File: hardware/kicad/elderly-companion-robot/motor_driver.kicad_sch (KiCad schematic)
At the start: 12 parts, among them J3 Motor_A, J4 Motor_B, U5 L298N

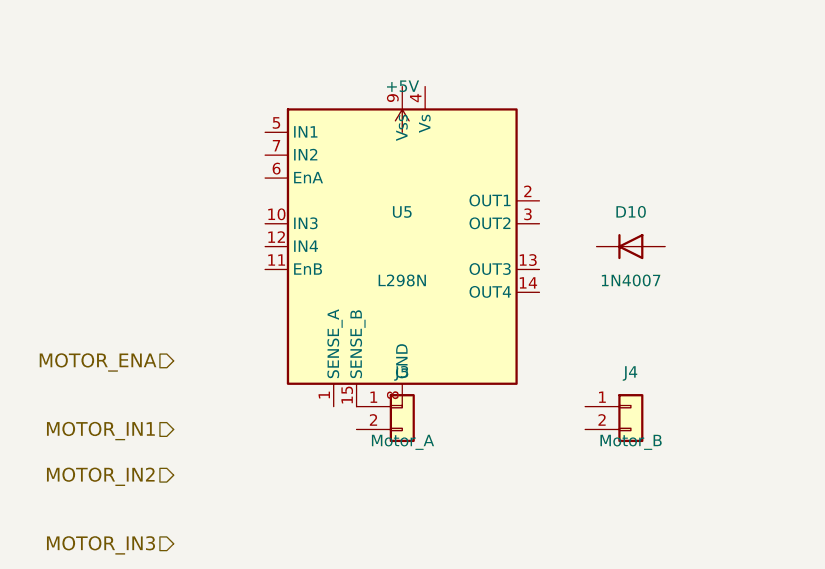
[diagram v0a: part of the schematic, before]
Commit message: Add net labels and signal connections across all schematic sheets
- MCU Core: Added net labels at all ESP32-S3 GPIO pin positions
  (I2C, I2S, motor, servo, IR, UART, ultrasonic signals)
- Added hierarchical labels for US_LEFT/RIGHT_TRIG/ECHO
- Remapped I2C_SCL to GPIO2 (GPIO22 not on WROOM-1 module)
- Remapped SERVO_PAN to GPIO42 (GPIO44 not available)
- Motor Driver: Added net labels at L298N input/output pins
- Sensors: Added I2C labels at MPU-6050 and SSD1306 pin positions
- Audio: Added I2S labels at MAX98357A and INMP441 connector
- Camera/Dock: Added UART, SIM_PWRKEY, servo, IR labels at SIM800C
- Added power symbols (+3V3, +5V, GND, +4V) across all sheets
- Boot circuit wiring started (EN pull-up, GPIO0 connections)
- ERC: 446 violations (mostly unconnected labels/pins - need wires)

Co-Authored-By: Claude Opus 4.7 <noreply@anthropic.com>
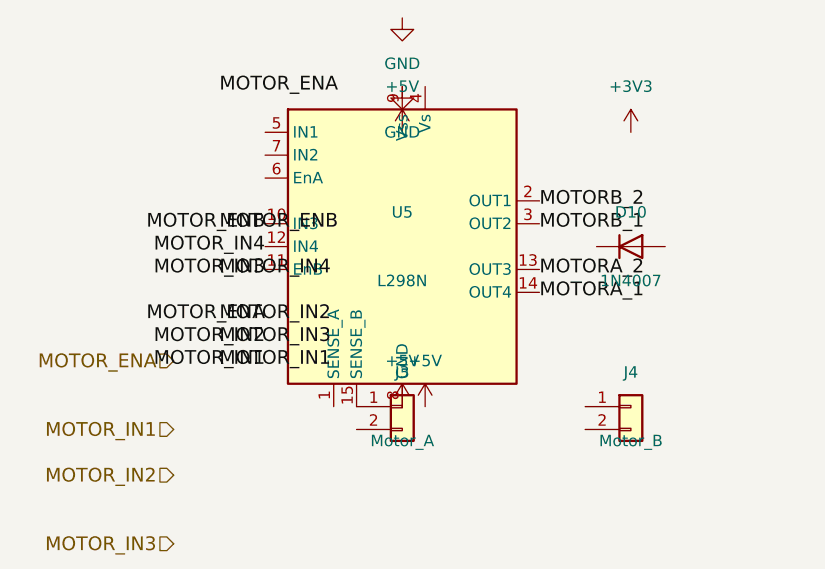
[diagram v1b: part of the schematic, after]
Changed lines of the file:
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@@
 	(version 20250114)
 	(generator "eeschema")
+	(generator_version "9.0")
 	(paper "A4")
 	(symbol
@@
 		(effects (font (size 1.524 1.524)))
 	)
+	(symbol
+		(lib_id "power:+5V")
+		(at 50.8 68.58 0)
+		(unit 1)
+		(exclude_from_sim no)
+		(in_bom yes)
+		(on_board yes)
+		(dnp no)
+		(property "Reference" "#PWR3f77"
+			(at 50.8 62.23 0)
+			(effects (font (size 1.27 1.27)) (hide yes))
+		)
+		(property "Value" "+5V"
+			(at 50.8 63.5 0)
+			(effects (font (size 1.27 1.27)))
+		)
+		(property "Footprint" ""
+			(at 50.8 68.58 0)
+			(effects (font (size 1.27 1.27)) (hide yes))
+		)
+		(property "Datasheet" "~"
+			(at 50.8 68.58 0)
+			(effects (font (size 1.27 1.27)) (hide yes))
+		)
+		(instances
+			(project "elderly-companion-robot"
+				(path "/4df18afa-6300-4e30-8425-a36b74deadc2"
+					(reference "#PWR3f77") (unit 1)
+				)
+			)
+		)
+	)
+	(symbol
+		(lib_id "power:+3V3")
+		(at 76.2 38.1 0)
+		(unit 1)
+		(exclude_from_sim no)
+		(in_bom yes)
+		(on_board yes)
+		(dnp no)
+		(property "Reference" "#PWR25e6"
+			(at 76.2 31.75 0)
+			(effects (font (size 1.27 1.27)) (hide yes))
+		)
+		(property "Value" "+3V3"
+			(at 76.2 33.02 0)
+			(effects (font (size 1.27 1.27)))
+		)
+		(property "Footprint" ""
+			(at 76.2 38.1 0)
+			(effects (font (size 1.27 1.27)) (hide yes))
+		)
+		(property "Datasheet" "~"
+			(at 76.2 38.1 0)
+			(effects (font (size 1.27 1.27)) (hide yes))
+		)
+		(instances
+			(project "elderly-companion-robot"
+				(path "/d9fcf0f2-e47a-435c-a687-ceb3313aee18"
+					(reference "#PWR25e6") (unit 1)
+				)
+			)
+		)
+	)
+	(symbol
+		(lib_id "power:GND")
+		(at 50.8 25.4 0)
+		(unit 1)
+		(exclude_from_sim no)
+		(in_bom yes)
+		(on_board yes)
+		(dnp no)
+		(property "Reference" "#PWR14a6"
+			(at 50.8 31.75 0)
+			(effects (font (size 1.27 1.27)) (hide yes))
+		)
+		(property "Value" "GND"
+			(at 50.8 30.48 0)
+			(effects (font (size 1.27 1.27)))
+		)
+		(property "Footprint" ""
+			(at 50.8 25.4 0)
+			(effects (font (size 1.27 1.27)) (hide yes))
+		)
+		(property "Datasheet" "~"
+			(at 50.8 25.4 0)
+			(effects (font (size 1.27 1.27)) (hide yes))
+		)
+		(instances
+			(project "elderly-companion-robot"
+				(path "/d9c6cb88-2fe3-4b29-b416-8258e6ea7698"
+					(reference "#PWR14a6") (unit 1)
+				)
+			)
+		)
+	)
+	(label "MOTOR_ENA"
+		(at 30.48 33.02 0)
+		(effects (font (size 1.524 1.524)))
+	)
+	(label "MOTOR_IN1"
+		(at 30.48 63.5 0)
+		(effects (font (size 1.524 1.524)))
+	)
+	(label "MOTOR_IN2"
+		(at 30.48 58.42 0)
+		(effects (font (size 1.524 1.524)))
+	)
+	(label "MOTOR_IN3"
+		(at 30.48 60.96 0)
+		(effects (font (size 1.524 1.524)))
+	)
+	(label "MOTOR_IN4"
+		(at 30.48 53.34 0)
+		(effects (font (size 1.524 1.524)))
+	)
+	(label "MOTOR_ENB"
+		(at 30.48 48.26 0)
+		(effects (font (size 1.524 1.524)))
+	)
+	(label "MOTOR_IN1"
+		(at 35.56 63.5 180)
+		(effects (font (size 1.524 1.524)))
+	)
+	(label "MOTOR_IN2"
+		(at 35.56 60.96 180)
+		(effects (font (size 1.524 1.524)))
+	)
+	(label "MOTOR_IN3"
+		(at 35.56 53.34 180)
+		(effects (font (size 1.524 1.524)))
+	)
+	(label "MOTOR_IN4"
+		(at 35.56 50.8 180)
+		(effects (font (size 1.524 1.524)))
+	)
+	(label "MOTOR_ENA"
+		(at 35.56 58.42 180)
+		(effects (font (size 1.524 1.524)))
+	)
+	(label "MOTOR_ENB"
+		(at 35.56 48.26 180)
+		(effects (font (size 1.524 1.524)))
+	)
+	(label "MOTORA_1"
+		(at 66.04 55.88 0)
+		(effects (font (size 1.524 1.524)))
+	)
+	(label "MOTORA_2"
+		(at 66.04 53.34 0)
+		(effects (font (size 1.524 1.524)))
+	)
+	(label "MOTORB_1"
+		(at 66.04 48.26 0)
+		(effects (font (size 1.524 1.524)))
+	)
+	(label "MOTORB_2"
+		(at 66.04 45.72 0)
+		(effects (font (size 1.524 1.524)))
+	)
+	(symbol
+		(lib_id "power:+5V")
+		(at 53.34 68.58 0)
+		(unit 1)
+		(exclude_from_sim no)
+		(in_bom yes)
+		(on_board yes)
+		(dnp no)
+		(property "Reference" "#PWRf70d"
+			(at 53.34 62.23 0)
+			(effects (font (size 1.27 1.27)) (hide yes))
+		)
+		(property "Value" "+5V"
+			(at 53.34 63.5 0)
+			(effects (font (size 1.27 1.27)))
+		)
+		(property "Footprint" ""
+			(at 53.34 68.58 0)
+			(effects (font (size 1.27 1.27)) (hide yes))
+		)
+		(property "Datasheet" "~"
+			(at 53.34 68.58 0)
+			(effects (font (size 1.27 1.27)) (hide yes))
+		)
+		(instances
+			(project "elderly-companion-robot"
+				(path "/31d9b13f-5923-4cd5-9096-a5c3c0de11a9"
+					(reference "#PWRf70d") (unit 1)
+				)
+			)
+		)
+	)
+	(symbol
+		(lib_id "power:GND")
+		(at 50.8 33.02 0)
+		(unit 1)
+		(exclude_from_sim no)
+		(in_bom yes)
+		(on_board yes)
+		(dnp no)
+		(property "Reference" "#PWR77bf"
+			(at 50.8 39.37 0)
+			(effects (font (size 1.27 1.27)) (hide yes))
+		)
+		(property "Value" "GND"
+			(at 50.8 38.1 0)
+			(effects (font (size 1.27 1.27)))
+		)
+		(property "Footprint" ""
+			(at 50.8 33.02 0)
+			(effects (font (size 1.27 1.27)) (hide yes))
+		)
+		(property "Datasheet" "~"
+			(at 50.8 33.02 0)
+			(effects (font (size 1.27 1.27)) (hide yes))
+		)
+		(instances
+			(project "elderly-companion-robot"
+				(path "/9a39cfae-f152-4277-b696-2ad675101116"
+					(reference "#PWR77bf") (unit 1)
+				)
+			)
+		)
+	)
 	(sheet_instances
